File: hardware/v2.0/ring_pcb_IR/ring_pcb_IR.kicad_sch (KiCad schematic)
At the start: 11 parts, among them Q1 Q_PNP_BEC, Q2 Q_PNP_BEC, Q3 Q_NPN_BEC, Q4 Q_NPN_BEC, Q5 Q_NPN_BEC, Q6 Q_NPN_BEC, U1 ATtiny85-20M

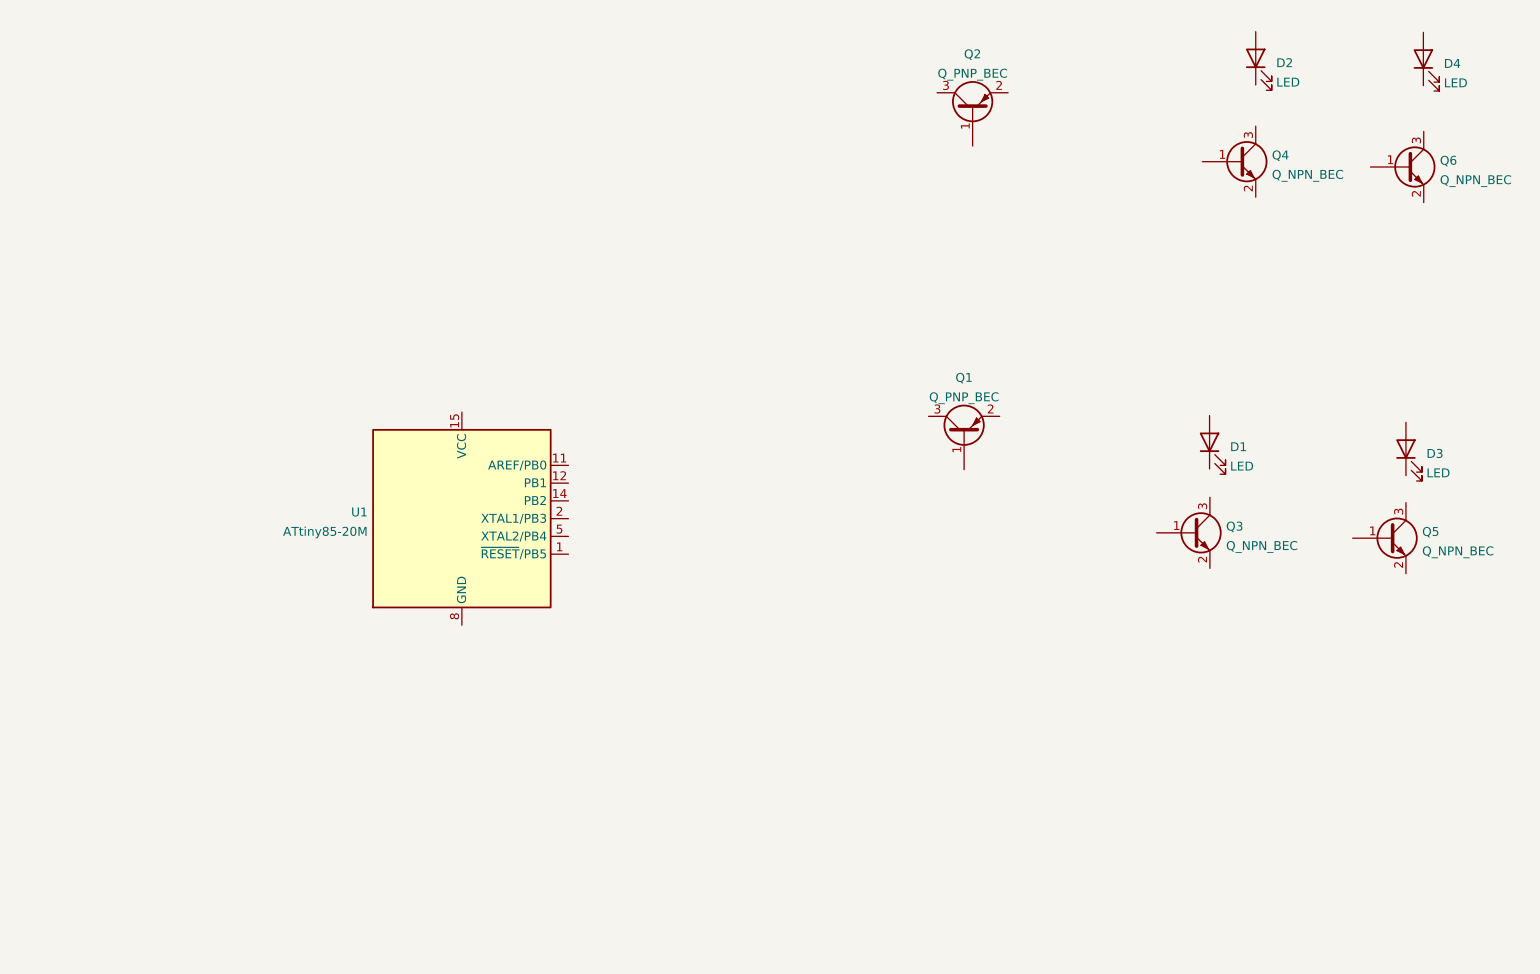
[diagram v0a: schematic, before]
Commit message: Start wiring up LED driver
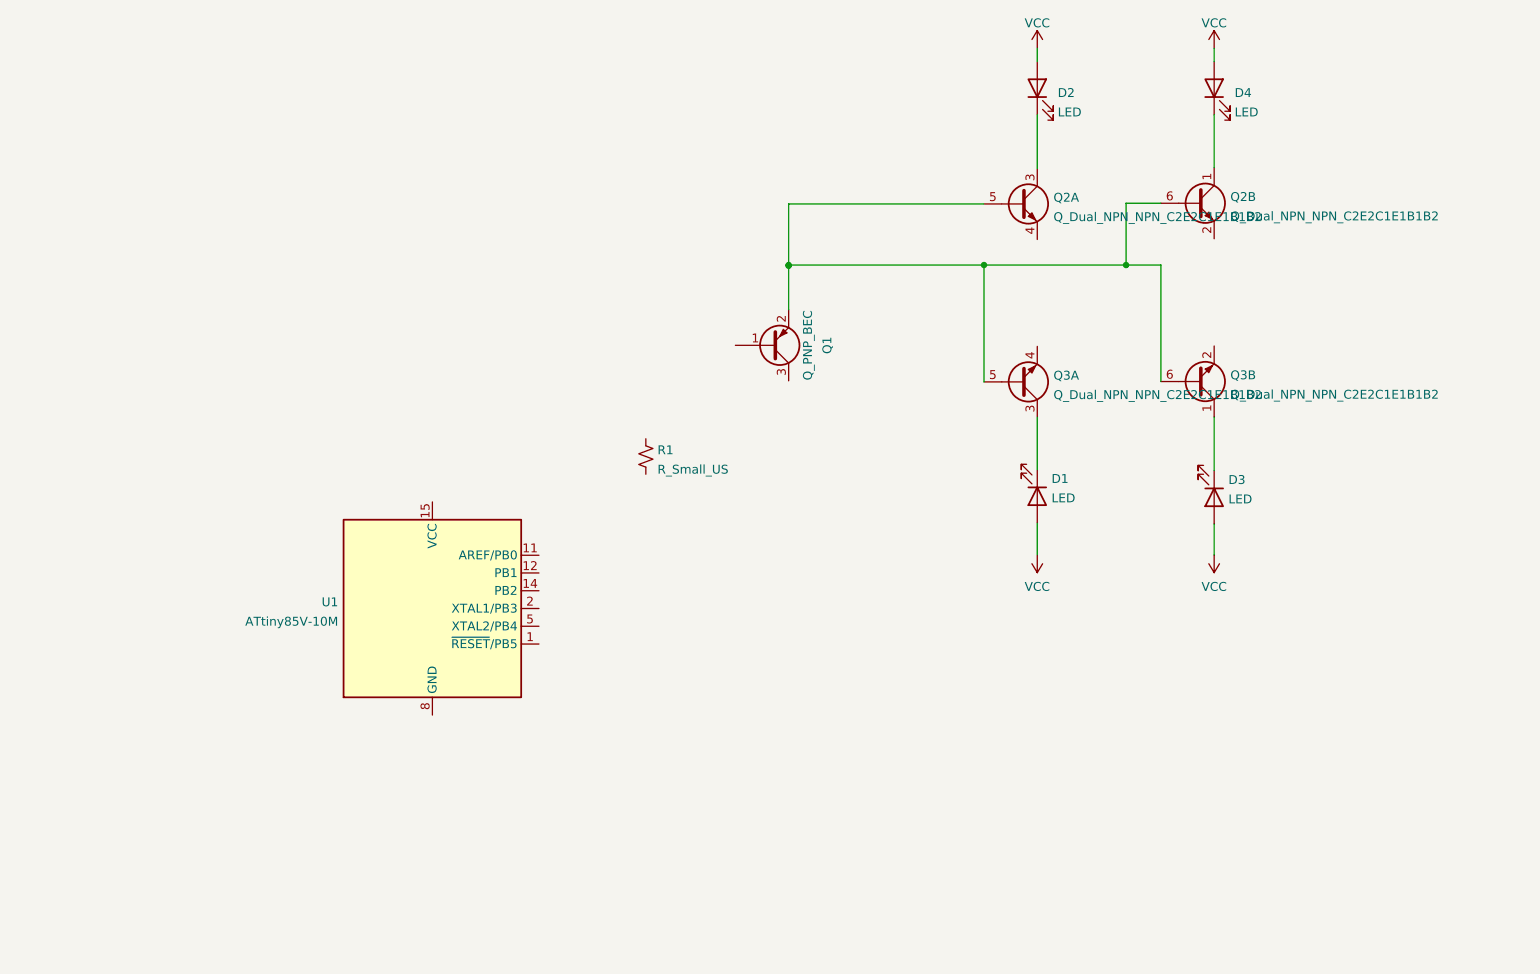
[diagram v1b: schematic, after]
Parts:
- removed Q2: Q_PNP_BEC, Package_TO_SOT_SMD:SOT-23, symbol Device:Q_PNP_BEC
- removed Q3, Q4, Q5, Q6: Q_NPN_BEC, Package_TO_SOT_SMD:SOT-23, symbol Device:Q_NPN_BEC
- removed U1: ATtiny85-20M, Package_DFN_QFN:QFN-20-1EP_4x4mm_P0.5mm_EP2.6x2.6mm, symbol MCU_Microchip_ATtiny:ATtiny85-20M
- added Q2, Q3: Q_Dual_NPN_NPN_C2E2C1E1B1B2, Package_TO_SOT_SMD:SOT-23-6, symbol Device:Q_Dual_NPN_NPN_C2E2C1E1B1B2
- added R1: R_Small_US, symbol Device:R_Small_US
- added U1: ATtiny85V-10M, Package_DFN_QFN:QFN-20-1EP_4x4mm_P0.5mm_EP2.6x2.6mm, symbol MCU_Microchip_ATtiny:ATtiny85V-10M
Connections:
- net at D4.1 (K): now also Q2.1 (C2)
- net VCC: now reaches D4.2 (A)
- net VCC: now also D1.2 (A), D2.2 (A), D3.2 (A)
- net at D2.1 (K): now also Q2.3 (C1)
- net at D3.1 (K): now also Q3.1 (C2)
- net at D1.1 (K): now also Q3.3 (C1)
- new net: Q2.5 (B1), Q2.6 (B2), Q3.5 (B1), Q3.6 (B2)
- new net: U1.21 (GND), U1.8 (GND)
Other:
- moved on the sheet: D1, D2, D3, D4, Q1

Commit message: Add IR components
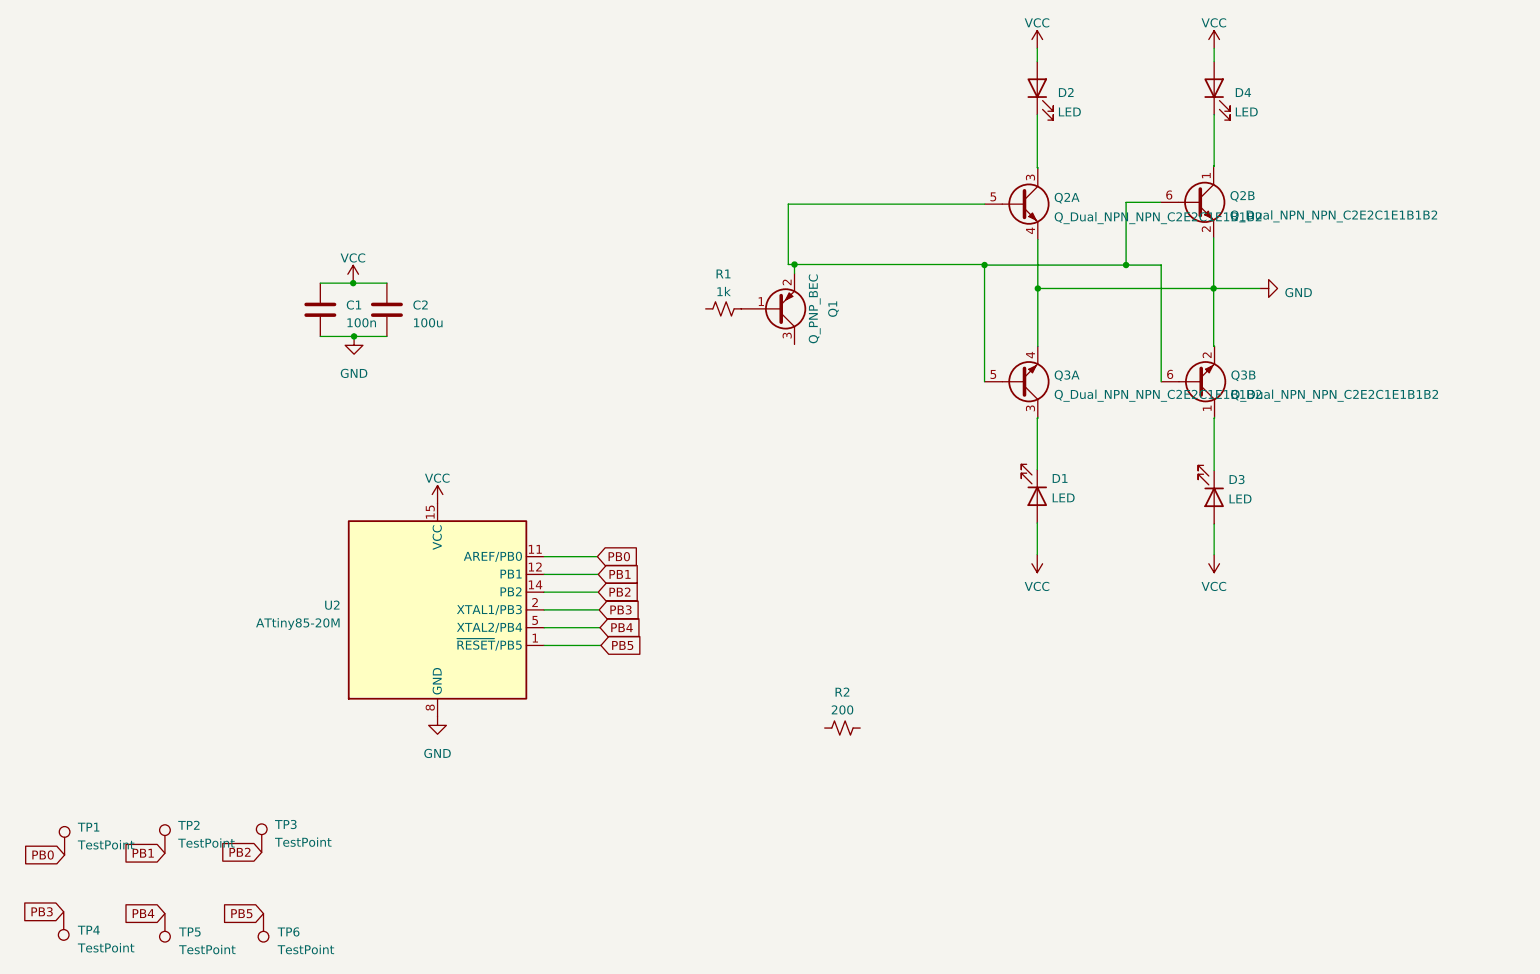
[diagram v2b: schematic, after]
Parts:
- removed U1: ATtiny85V-10M, Package_DFN_QFN:QFN-20-1EP_4x4mm_P0.5mm_EP2.6x2.6mm, symbol MCU_Microchip_ATtiny:ATtiny85V-10M
- added C1: 100n, Capacitor_SMD:C_0603_1608Metric, symbol Device:C
- added C2: 100u, Capacitor_SMD:C_0603_1608Metric, symbol Device:C
- added R2: 200, Resistor_SMD:R_0603_1608Metric, symbol Device:R_Small_US
- added TP1, TP2, TP3, TP4, TP5, TP6: TestPoint, TestPoint:TestPoint_Pad_1.0x1.0mm, symbol Connector:TestPoint
- added U2: ATtiny85-20M, Package_DFN_QFN:QFN-20-1EP_4x4mm_P0.5mm_EP2.6x2.6mm, symbol MCU_Microchip_ATtiny:ATtiny85-20M
- R1: value R_Small_US -> 1k; footprint (none) -> Resistor_SMD:R_0603_1608Metric
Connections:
- net VCC: now also C1.1, C2.1, U2.15 (VCC)
- net at R1.2: now also Q1.1 (B)
- net GND: now reaches Q2.2 (E2)
- net GND: now also Q2.4 (E1), Q3.2 (E2), Q3.4 (E1), C1.2, C2.2, U2.21 (GND), U2.8 (GND)
- net at Q2.5 (B1), Q2.6 (B2), Q3.5 (B1)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: now also Q1.2 (E)
- new net PB0: TP1.1, U2.11 (AREF/PB0)
- new net PB1: TP2.1, U2.12 (PB1)
- new net PB2: TP3.1, U2.14 (PB2)
- new net PB3: TP4.1, U2.2 (XTAL1/PB3)
- new net PB4: TP5.1, U2.5 (XTAL2/PB4)
- new net PB5: TP6.1, U2.1 (~{RESET}/PB5)
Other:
- moved on the sheet: Q1, R1
